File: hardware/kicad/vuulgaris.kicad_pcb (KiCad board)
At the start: 2 copper layers, 284.3 x 125 mm, 46 parts, among them J1 TFPUSH, J10 PJ-603_C41409498, J2 PJ-376, J3 PJ-376, J4 PJ-376, J5 PJ-376, J7 PJ-603_C41409498, J8 PJ-603_C41409498, J9 PJ-603_C41409498, SW4 CPG151101S03, SW5 CPG151101S03, SW6 CPG151101S03, SW7 CPG151101S03, U1 ES_DAISY_PATCH_SM_REV1, U3 MCP23017-E_SO, U4 MCP23017-E_SO, U5 AMS1117-3.3, U6 AMS1117-3.3

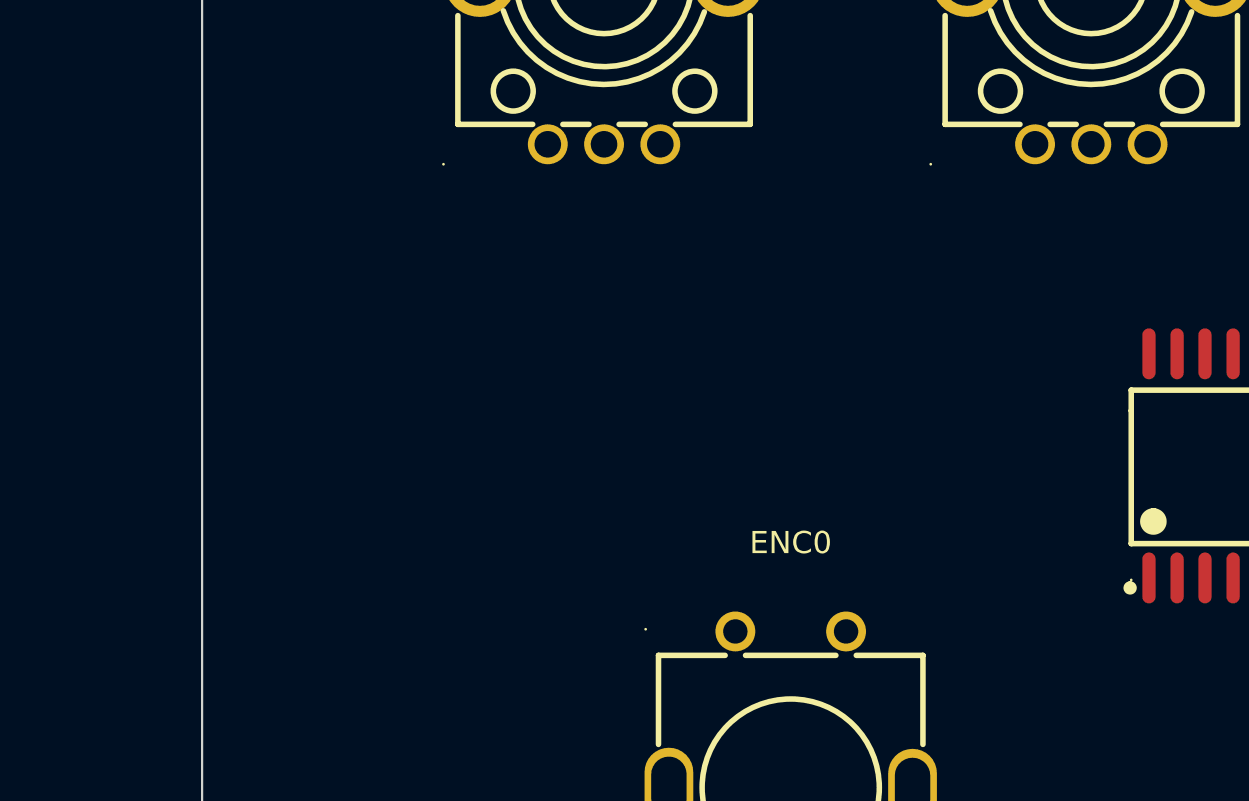
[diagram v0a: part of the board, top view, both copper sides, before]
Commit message: hardware: place the power input stage in the left-edge pocket
All 15 parts placed on the front, x 3..40, y 41..64 -- the one region of the board
outside the capacitive electrodes, which span x 54-270, and diagonally opposite the
audio path in the top-right quadrant.

  J11  (3.8, 48)   barrel tip lands at x -7.00, flush with the wall's outer face
  D1 L1 C29 C30 D3   y 45, the input chain left to right
  L2 C31 C32 D2      y 51, the output chain
  C28 U7             y 59, the two tall through-hole parts
  R22-R24            x 39.5, the bleeder string

Two collisions found and fixed while placing. The first row sat at y 41 and clashed
with ENC2 and ENC4, whose pads reach y 41.4 -- the encoder bank extends further down
than the body outlines suggest. The bleeder and D2 landed on U3, the expander at
x 42-60. Both were caught by the pad-overlap check rather than by eye.

Verified: 184 non-circular pads at library orientation, 0 pad overlaps, no same-face
body overlaps, all 20 panel parts on their holes, nothing outside the outline.
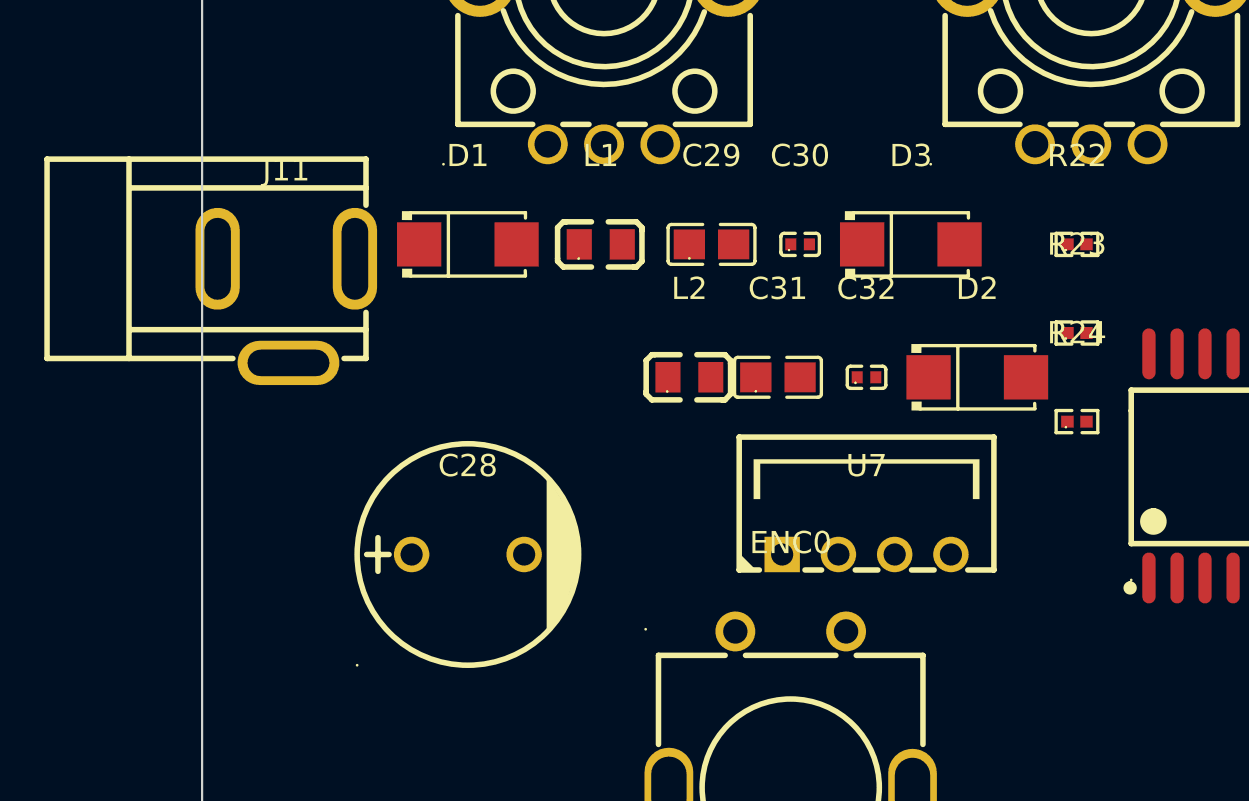
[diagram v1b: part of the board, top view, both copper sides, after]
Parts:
- added C28: 25YXJ470M10X12.5, vuulgaris:CAP-TH_BD10.0-P5.00-D1.0-FD, F.Cu at (112.0, 109.0)
- added C29: CL21A106KAYNNNE, vuulgaris:C0805, F.Cu at (123.0, 95.0)
- added C30: CL05B104KO5NNNC, vuulgaris:C0402, F.Cu at (127.0, 95.0)
- added C31: CL21A106KAYNNNE, vuulgaris:C0805, F.Cu at (126.0, 101.0)
- added C32: CL05B104KO5NNNC, vuulgaris:C0402, F.Cu at (130.0, 101.0)
- added D1: SS34_C8678, vuulgaris:SMA_L4.3-W2.6-LS5.2-RD, F.Cu at (112.0, 95.0)
- added D2: SS34_C8678, vuulgaris:SMA_L4.3-W2.6-LS5.2-RD, F.Cu at (135.0, 101.0)
- added D3: SS34_C8678, vuulgaris:SMA_L4.3-W2.6-LS5.2-RD, F.Cu at (132.0, 95.0)
- added J11: DC-005-20A, vuulgaris:DC-IN-TH_DC005, F.Cu at (103.8, 98.0)
- added L1: CMP201209UD4R7MT, vuulgaris:L0805, F.Cu at (118.0, 95.0)
- added L2: CMP201209UD4R7MT, vuulgaris:L0805, F.Cu at (122.0, 101.0)
- added R22: 0402WGF2201TCE, vuulgaris:R0402, F.Cu at (139.5, 95.0)
- added R23: 0402WGF2201TCE, vuulgaris:R0402, F.Cu at (139.5, 99.0)
- added R24: 0402WGF2201TCE, vuulgaris:R0402, F.Cu at (139.5, 103.0)
- added U7: B1212S-1WR3_C3031174, vuulgaris:PWRM-TH_4P-L11.5-W6.1-P2.54_1, F.Cu at (130.0, 109.0)

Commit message: hardware: power stage to the back, right of the 1/4in jacks
The audio jacks shift left to open the space: J7/J8 into the RV1-to-OLED window at
x 163-194, J9/J10 hard left under the OLED at x 206-235. They cannot be one run --
the OLED's 9-pin column at x 202.75-205.55 is a wall through the middle of the top
edge.

The power stage follows them on B.Cu, x 240-277, y 14-42, under the OLED. It had to
go to the back: the front is fully committed there, with the OLED body down to y 47.6
and the Daisy from y 54. That also fixes the height worry from the previous placement
-- C28's 12.5mm can was marginal against the ~12-13mm faceplate gap -- and puts the
switching module on the opposite face from the touch electrodes.

J11 sits at x 245 with its barrel exiting the TOP wall, tip at y -7.00. It was first
placed at x 276 in the gap past the OLED's right mounting hole, but that window is
only 9.2mm for a 9mm part and its pads clipped the hole; shifting clear ran it off
the right edge of the board.

Two checker fixes came out of this. "outside board outline" only ever tested
footprint ORIGINS, so J11 hanging 3.5mm over the right edge passed silently -- there
is now a real body-vs-outline check, with the nine jacks exempted since their barrels
deliberately protrude through the wall. And that check initially flagged 38 parts
because it compared sheet coordinates against board dimensions.

Verified: 181 non-circular pads at library orientation, 0 pad overlaps, no same-face
body overlaps, all bodies inside the outline, all 20 panel parts on their holes.
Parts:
- C28, C29, C30, C31, C32, D1, D2, D3, J11, L1, L2, R22, R23, R24, U7: moved to B.Cu
- moved D1 261.6 mm to (372.0, 66.0), turned to 180 degrees
- moved L1 248.7 mm to (365.0, 66.0), turned to 180 degrees
- moved J11 245.2 mm to (345.0, 53.8), turned to 270 degrees
- moved C29 238.8 mm to (360.0, 66.0), turned to 180 degrees
- moved C28 236.0 mm to (346.0, 78.0), turned to 180 degrees
- moved U7 233.8 mm to (362.0, 80.0), turned to 180 degrees
- moved R24 231.0 mm to (370.0, 88.0), turned to 180 degrees
- moved C30 230.8 mm to (356.0, 66.0), turned to 180 degrees
- moved L2 228.4 mm to (350.0, 88.0), turned to 180 degrees
- moved R23 227.8 mm to (367.0, 88.0), turned to 180 degrees
- moved R22 224.6 mm to (364.0, 88.0), turned to 180 degrees
- moved D2 221.4 mm to (356.0, 88.0), turned to 180 degrees
- moved D3 220.9 mm to (351.0, 66.0), turned to 180 degrees
- moved C31 219.4 mm to (345.0, 88.0), turned to 180 degrees
- moved C32 211.4 mm to (341.0, 88.0), turned to 180 degrees
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
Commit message: hardware: move the power inlet away from the audio jacks
J11 was 6.85mm from J10, the nearest 1/4in jack. Moved to the right-hand end of the
same window: now 23.85mm.

Two reasons it matters more than the schematic suggests. The DC cable from a
switching brick runs alongside the audio cables OUTSIDE the enclosure, where nothing
on the board can shield it. And the +12V input trace carries whatever ripple the
brick produces until it reaches the bulk cap, so it is the noisiest net here.

It also puts the inlet beside U7 (x 256.25-267.75), which is the actual switching
source at 260kHz. Clustering the noisy section at the right-hand end leaves the whole
audio group at x 163-235 clear of it.

The far-right window past the OLED's right mounting hole is still unusable -- 9.2mm
for a 9mm part, and J11's pads clipped the hole.

Verified: 181 pads at library orientation, 0 pad overlaps, no same-face body
overlaps, all bodies inside the outline, and 0 overlapping flashes across both
copper layers.
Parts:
- moved J11 16.0 mm to (361.0, 53.8)
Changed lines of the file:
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@@
   )
   (footprint "vuulgaris:DC-IN-TH_DC005" (layer "B.Cu")
-    (at 345.0 53.8 270)
+    (at 361.0 53.8 270)
     (property "Sheetfile" "vuulgaris.kicad_sch")
     (property "Sheetname" "")

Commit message: hardware: J11 pad was 0.30mm over the board edge
Pad 2 ran to y -0.30 against a top edge at y 0. The outline is milled, so that pad
would have been cut through. Moved J11 down 1.2mm; pad 2 now starts at y +0.90.

The barrel tip goes from y -7.00 to -5.80, so it now sits 4.80mm into the 6mm wall
rather than flush with its outer face. Still well within a clearance hole and easily
reached by a plug.

The checker missed it because EDGE_OK exempted the whole of J11 from the
body-vs-outline test -- correct for the barrel, which is meant to overhang, but it
took the pads with it. Pads may never cross the outline, so there is now a separate
pad-vs-outline check with no exemptions at all.

That is the third gap found in this check in two days: it originally tested only
footprint origins, then compared sheet coordinates against board dimensions, and now
this. Bodies and pads are tested separately because they have different rules.

Verified: pads inside the outline all, bodies inside the outline all, 0 pad overlaps,
no same-face body overlaps, 181 pads at library orientation, all 20 panel parts on
their holes.
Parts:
- moved J11 1.20 mm to (361.0, 55.0)
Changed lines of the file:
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@@
   )
   (footprint "vuulgaris:DC-IN-TH_DC005" (layer "B.Cu")
-    (at 361.0 53.8 270)
+    (at 361.0 55.0 270)
     (property "Sheetfile" "vuulgaris.kicad_sch")
     (property "Sheetname" "")

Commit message: hardware: J11 pad really was over the edge, and add a Gerber-based check
The pad was still 0.40mm past the milled outline after the previous "fix", and
place.py reported it clean both times.

Root cause: KiCad REWRITES a footprint's local pad coordinates when you flip it --
negating local Y and swinging pad angles 180. J11's library pads are at y -2.35,
-2.35, +2.35; on the board they are +2.35, +2.35, -2.35. Every calculation here
assumed the library values, so the pads were computed in the wrong place. place.py
uses the same arithmetic that positioned the part, so it agreed with the mistake.

J11 moved y 5.0 -> 6.2. The barrel tip is now 3.6mm into the 6mm wall, still well
inside a clearance hole.

tools/gerbercheck.py is the response to the pattern. Gerbers are KiCad's output,
not this repo's arithmetic, so they cannot share the error: aperture definitions
carry the true pad size and orientation, flash coordinates the true position. It
checks that no flash crosses Edge.Cuts and that no two flashes on a layer overlap.

That is the third failure of the same kind. Rotated parts were once bounded with
their unrotated extents, 28mm out on U1. The outline test compared only footprint
origins, so J11 hung 3.5mm over and passed. Now this. Each time the check and the
placement shared a transform, and each time the answer was "clean".

  python3 tools/gerbercheck.py     ->  CLEAN

Run it after anything is flipped or rotated, and before plotting fab files.
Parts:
- moved J11 1.20 mm to (361.0, 56.2)
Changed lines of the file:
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@@
   )
   (footprint "vuulgaris:DC-IN-TH_DC005" (layer "B.Cu")
-    (at 361.0 55.0 270)
+    (at 361.0 56.2 270)
     (property "Sheetfile" "vuulgaris.kicad_sch")
     (property "Sheetname" "")

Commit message: hardware: move the Daisy to the bottom wall, power stage down the right edge
The DKM10E-12 is 25.4mm square and through-hole. The B1212S it replaced was
11.5 x 6.1mm and lived under the OLED without complaint; this one cannot.

Worth being precise about what actually had to move. Only two parts in the power
stage have through-hole pins -- U7 and the USB-C's four shell legs. The other 21
are SMD on the back, and the screen is on the front, so the board separates them
and they stay put. It was never the parts under the screen, it was the pins
coming through it.

What decides the rest is a constraint that was not written down anywhere: the
capacitive scrub pads cover pcb x 54-270, y 57.5-124.5, which is the lower two
thirds of the board. Above that band the only 25.4mm-square opening is the OLED
itself, so U7 goes under the screen or under the electrodes, and there is no
third option at 284 x 125. Under the screen fails hard -- pins against a standoff
whose height nobody has measured, and it either assembles or it does not. Under
the electrodes fails soft, is mitigated by the faceplate's L3 hatched ground and
by the DKM being an encapsulated brick, and is where the Daisy has been sitting
all along. So U7 takes the right edge and the Daisy takes the bottom wall.

U1 rotates 90 -> 0, which is safe to do by text edit here only because all forty
of its pads are through-hole circles -- there are no pad shapes to swing, so the
failure that fused nine SD contacts into one bar cannot recur on this part.

U7 clears the OLED by 1.66mm and the board edge by 1.60mm. J1 follows the Daisy
so the SDIO run stays short.

Two rotations are provisional and flagged in design-state: U1's, because the
carrier footprint does not mark the micro-USB, and J11's, because the USB-C slot
has 0.17mm to the board edge and 0.62mm to the OLED. Neither gets settled by
arithmetic.
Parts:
- removed D3: SS34_C8678, vuulgaris:SMA_L4.3-W2.6-LS5.2-RD
- added C33: RVT1E470M0505_C2977553, vuulgaris:CAP-SMD_BD5.0-L5.3-W5.3-LS6.3-FD, F.Cu at (347.0, 116.0)
- added C34: CC0603JRX7R8BB104, vuulgaris:C0603, F.Cu at (347.0, 107.0)
- added C35: CC0603JRX7R8BB104, vuulgaris:C0603, F.Cu at (347.0, 120.0)
- added C36: RVT1H220M0605, vuulgaris:CAP-SMD_BD6.3-L6.6-W6.6-FD, F.Cu at (355.0, 130.0)
- added C37: RVT1H220M0605, vuulgaris:CAP-SMD_BD6.3-L6.6-W6.6-FD, F.Cu at (355.0, 140.0)
- added C38: CC0603JRX7R8BB104, vuulgaris:C0603, F.Cu at (355.0, 135.0)
- added C39: CC0603JRX7R8BB104, vuulgaris:C0603, F.Cu at (355.0, 145.0)
- added F1: ASMD1812-200, vuulgaris:F1812, F.Cu at (377.0, 64.0)
- added R25: RT0603BRD072K2L, vuulgaris:R0603, F.Cu at (362.0, 140.0)
- C28: value 25YXJ470M10X12.5 -> CC0603JRNPO9BN103; footprint vuulgaris:CAP-TH_BD10.0-P5.00-D1.0-FD -> vuulgaris:C0603
- C29: value CL21A106KAYNNNE -> RVT1H220M0605; footprint vuulgaris:C0805 -> vuulgaris:CAP-SMD_BD6.3-L6.6-W6.6-FD
- C30: value CL05B104KO5NNNC -> CC0805KKX7R9BB105; footprint vuulgaris:C0402 -> vuulgaris:C0805
- C31: value CL21A106KAYNNNE -> CC0603JRX7R8BB104; footprint vuulgaris:C0805 -> vuulgaris:C0603
- C32: value CL05B104KO5NNNC -> RVT1E470M0505_C2977553; footprint vuulgaris:C0402 -> vuulgaris:CAP-SMD_BD5.0-L5.3-W5.3-LS6.3-FD
- D1, D2: value SS34_C8678 -> YLED0402Y; footprint vuulgaris:SMA_L4.3-W2.6-LS5.2-RD -> vuulgaris:LED0402-R-RD
- J11: value DC-005-20A -> TYPE-C-31-M-12; footprint vuulgaris:DC-IN-TH_DC005 -> vuulgaris:USB-C_SMD-TYPE-C-31-M-12_1
- L1, L2: value CMP201209UD4R7MT -> BLM18PG121SN1D_C14709; footprint vuulgaris:L0805 -> vuulgaris:L0603
- R22, R23: value 0402WGF2201TCE -> RT0603BRD075K1L; footprint vuulgaris:R0402 -> vuulgaris:R0603
- R24: value 0402WGF2201TCE -> RT0603BRD072K2L; footprint vuulgaris:R0402 -> vuulgaris:R0603
- U7: value B1212S-1WR3_C3031174 -> DKM10E-12; footprint vuulgaris:PWRM-TH_4P-L11.5-W6.1-P2.54_1 -> vuulgaris:PWRM-TH_DKMW30F-12
- moved U1 184.1 mm to (180.0, 153.0), turned to 0 degrees
- moved J1 105.5 mm to (226.5, 143.4)
- moved D1 64.3 mm to (366.0, 130.0)
- moved D2 53.0 mm to (366.0, 140.0)
- moved L1 48.5 mm to (347.0, 111.0)
- moved R24 42.8 mm to (362.0, 130.0)
- moved L2 36.1 mm to (347.0, 124.0)
- moved C31 34.8 mm to (378.0, 77.0)
- moved U7 33.0 mm to (370.0, 112.0)
- moved C28 31.6 mm to (372.0, 60.0)
- moved R22 28.2 mm to (367.0, 60.0)
- moved R23 25.0 mm to (367.0, 63.0)
- moved C30 23.4 mm to (378.0, 74.0)
- moved J11 18.3 mm to (379.2, 54.0)
- moved C32 15.2 mm to (347.0, 102.0)
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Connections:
- C28 pad 1: /POS12V -> /VBUS
- C29 pad 1: /POS12V -> /VBUS_F
- C30 pad 1: /POS12V -> /GND
- C30 pad 2: /GND -> /VBUS_F
- C31 pad 1: /NEG12V -> /GND
- C31 pad 2: /GND -> /VBUS_F
- C32 pad 1: /NEG12V -> /POS12V_RAW
- D1 pad 1: /VIN_F -> /LED_POS
- D1 pad 2: /VIN_RAW -> /GND
- D2 pad 2: /NEG12V -> /LED_NEG
- J11 pad 1: /VIN_RAW -> /GND
- J11 pad 3: unconnected-(J11-Pad3) -> /GND
- L1 pad 1: /VIN_F -> /POS12V_RAW
- L2 pad 1: /VNEG_RAW -> /NEG12V_RAW
- R22 pad 1: /NEG12V -> /CC1
- R22 pad 2: /BLEED_A -> /GND
- R23 pad 1: /BLEED_A -> /GND
- R23 pad 2: /BLEED_B -> /CC2
- R24 pad 1: /BLEED_B -> /LED_POS
- R24 pad 2: /GND -> /POS12V
- U7 pad 1: /GND -> /VBUS_F
- U7 pad 2: /POS12V -> /GND
- U7 pad 3: /VNEG_RAW -> /POS12V_RAW
